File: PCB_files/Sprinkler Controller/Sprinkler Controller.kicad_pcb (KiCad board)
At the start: 2 copper layers, 1 part, among them U1 ESP32_DevKit_V1_DOIT

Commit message: progress on PCB
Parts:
- added BR1: DF04S, Bridge_rectifier:SOP510P1040X260-4N, F.Cu at (116.3, 89.0)
- added C1: 1000 uF, Capacitor_THT:CP_Radial_D12.5mm_P5.00mm, F.Cu at (115.0, 99.3)
- added D1: SS34, Diode_SMD:D_SMA, F.Cu at (131.0, 103.8)
- added J1: Screw_Terminal_01x02, TerminalBlock_MetzConnect:TerminalBlock_MetzConnect_Type094_RT03502HBLU_1x02_P5.00mm_Horizontal, F.Cu at (104.0, 87.0)
- added J2: Screw_Terminal_01x11, TerminalBlock_Phoenix:TerminalBlock_Phoenix_MKDS-1,5-11_1x11_P5.00mm_Horizontal, F.Cu at (159.5, 146.5)
- added L1: 33uH, Inductor_SMD:L_Vishay_IHLP-5050, F.Cu at (145.5, 89.8)
- added RN1: 4816P-T02-681LF, Resistor_Network:SOIC127P762X240-16N, F.Cu at (173.0, 121.5)
- added RN2: 4816P-T02-681LF, Resistor_Network:SOIC127P762X240-16N, F.Cu at (197.0, 121.5)
- added U10: ~, SSR:OR-M4XXA, F.Cu at (202.0, 132.5)
- added U11: ~, SSR:OR-M4XXA, F.Cu at (207.0, 132.5)
- added U12: LM2596S-ADJ, Package_TO_SOT_SMD:TO-263-5_TabPin3, F.Cu at (130.1, 90.1)
- added U2: ~, SSR:OR-M4XXA, F.Cu at (162.0, 132.5)
- added U3: ~, SSR:OR-M4XXA, F.Cu at (167.0, 132.5)
- added U4: ~, SSR:OR-M4XXA, F.Cu at (172.0, 132.5)
- added U5: ~, SSR:OR-M4XXA, F.Cu at (177.0, 132.5)
- added U6: ~, SSR:OR-M4XXA, F.Cu at (182.0, 132.5)
- added U7: ~, SSR:OR-M4XXA, F.Cu at (187.0, 132.5)
- added U8: ~, SSR:OR-M4XXA, F.Cu at (192.0, 132.5)
- added U9: ~, SSR:OR-M4XXA, F.Cu at (197.0, 132.5)
- moved U1 42.2 mm to (164.3, 97.5), turned to 90 degrees
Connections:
- U1 pad 10: unconnected-(U1-IO27-Pad10) -> Net-(U1-IO27)
- U1 pad 11: unconnected-(U1-IO14-Pad11) -> Net-(U1-IO14)
- U1 pad 13: unconnected-(U1-IO13-Pad13) -> Net-(U1-IO13)
- U1 pad 24: unconnected-(U1-IO18-Pad24) -> Net-(U1-IO18)
- U1 pad 25: unconnected-(U1-IO19-Pad25) -> Net-(U1-IO19)
- U1 pad 26: unconnected-(U1-IO21-Pad26) -> Net-(U1-IO21)
- U1 pad 6: unconnected-(U1-IO32-Pad6) -> Net-(U1-IO32)
- U1 pad 7: unconnected-(U1-IO33-Pad7) -> Net-(U1-IO33)
- U1 pad 8: unconnected-(U1-IO25-Pad8) -> Net-(U1-IO25)
- U1 pad 9: unconnected-(U1-IO26-Pad9) -> Net-(U1-IO26)
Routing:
- net Net-(U1-IO27): track 0.00 -> 18.2 mm, vias 0 -> 1
- net Net-(U1-IO26): track 0.00 -> 17.0 mm
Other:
- board outline added: 116 x 72 mm

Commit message: board complete
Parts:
- added C2: 220uF, Capacitor_THT:CP_Radial_D10.0mm_P5.00mm, F.Cu at (152.5, 99.6)
- added C3: 0.1uF, Capacitor_SMD:C_0603_1608Metric, F.Cu at (123.5, 104.2)
- added C4: 0.0033uF, Capacitor_SMD:C_0402_1005Metric, F.Cu at (136.5, 98.5)
- added C5: 0.1uF, Capacitor_SMD:C_0603_1608Metric, F.Cu at (138.0, 99.0)
- added D10: LED, LED_SMD:LED_0402_1005Metric, F.Cu at (197.0, 130.0)
- added D11: LED, LED_SMD:LED_0402_1005Metric, F.Cu at (202.0, 130.0)
- added D12: LED, LED_SMD:LED_0402_1005Metric, F.Cu at (207.0, 130.0)
- added D2: LED, LED_SMD:LED_0402_1005Metric, F.Cu at (146.0, 105.5)
- added D3: LED, LED_SMD:LED_0402_1005Metric, F.Cu at (162.0, 130.0)
- added D4: LED, LED_SMD:LED_0402_1005Metric, F.Cu at (167.0, 130.0)
- added D5: LED, LED_SMD:LED_0402_1005Metric, F.Cu at (172.0, 130.0)
- added D6: LED, LED_SMD:LED_0402_1005Metric, F.Cu at (177.0, 130.0)
- added D7: LED, LED_SMD:LED_0402_1005Metric, F.Cu at (182.0, 130.0)
- added D8: LED, LED_SMD:LED_0402_1005Metric, F.Cu at (187.0, 130.0)
- added D9: LED, LED_SMD:LED_0402_1005Metric, F.Cu at (192.0, 130.0)
- added R1: 510, Resistor_SMD:R_0805_2012Metric, F.Cu at (137.0, 105.4)
- added R2: 1k, Resistor_SMD:R_1206_3216Metric, F.Cu at (146.0, 100.0)
- added RV1: 10k, Potentiometer:RES3_PV36W103C01B00_BRN, F.Cu at (142.0, 105.0)
- moved J2 0.50 mm to (159.0, 146.5)
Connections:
- BR1 pad 2: Net-(BR1--) -> GND
- BR1 pad 3: Net-(BR1-~_1) -> AC
- BR1 pad 4: Net-(BR1-~_2) -> GNDPWR
- C1 pad 2: Net-(BR1--) -> GND
- D1 pad 2: Net-(BR1--) -> GND
- J1 pad 1: Net-(BR1-~_1) -> AC
- J1 pad 2: Net-(BR1-~_2) -> GNDPWR
- J2 pad 11: Net-(BR1-~_1) -> GNDPWR
- L1 pad 2: unconnected-(L1-Pad2) -> VCC
- RN1 pad 11: Net-(U6-Input+) -> Net-(D7-A)
- RN1 pad 12: Net-(U5-Input+) -> Net-(D6-A)
- RN1 pad 13: Net-(U4-Input+) -> Net-(D5-A)
- RN1 pad 14: Net-(U3-Input+) -> Net-(D4-A)
- RN1 pad 15: Net-(U2-Input+) -> Net-(D3-A)
- RN2 pad 11: Net-(U11-Input+) -> Net-(D12-A)
- RN2 pad 12: Net-(U10-Input+) -> Net-(D11-A)
- RN2 pad 13: Net-(U9-Input+) -> Net-(D10-A)
- RN2 pad 14: Net-(U8-Input+) -> Net-(D9-A)
- RN2 pad 15: Net-(U7-Input+) -> Net-(D8-A)
- U1 pad 14: unconnected-(U1-GND-Pad14) -> GND
- U1 pad 15: unconnected-(U1-VIN-Pad15) -> VCC
- U1 pad 17: unconnected-(U1-GND-Pad17) -> GND
- U10 pad 1: Net-(U10-Input+) -> Net-(D11-K)
- U10 pad 3: Net-(BR1-~_2) -> AC
- U11 pad 1: Net-(U11-Input+) -> Net-(D12-K)
- U11 pad 3: Net-(BR1-~_2) -> AC
- U12 pad 3: Net-(BR1--) -> GND
- U12 pad 4: unconnected-(U12-FB-Pad4) -> Net-(U12-FB)
- U12 pad 5: Net-(BR1--) -> GND
- U2 pad 1: Net-(U2-Input+) -> Net-(D3-K)
- U2 pad 3: Net-(BR1-~_2) -> AC
- U3 pad 1: Net-(U3-Input+) -> Net-(D4-K)
- U3 pad 3: Net-(BR1-~_2) -> AC
- U4 pad 1: Net-(U4-Input+) -> Net-(D5-K)
- U4 pad 3: Net-(BR1-~_2) -> AC
- U5 pad 1: Net-(U5-Input+) -> Net-(D6-K)
- U5 pad 3: Net-(BR1-~_2) -> AC
- U6 pad 1: Net-(U6-Input+) -> Net-(D7-K)
- U6 pad 3: Net-(BR1-~_2) -> AC
- U7 pad 1: Net-(U7-Input+) -> Net-(D8-K)
- U7 pad 3: Net-(BR1-~_2) -> AC
- U8 pad 1: Net-(U8-Input+) -> Net-(D9-K)
- U8 pad 3: Net-(BR1-~_2) -> AC
- U9 pad 1: Net-(U9-Input+) -> Net-(D10-K)
- U9 pad 3: Net-(BR1-~_2) -> AC
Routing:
- net GNDPWR: track 0.00 -> 152.5 mm
- net GND: track 0.00 -> 103.2 mm, vias 0 -> 5
- net VCC: track 0.00 -> 82.4 mm, vias 0 -> 1
- net Net-(U1-IO19): track 0.00 -> 76.7 mm, vias 0 -> 2
- net Net-(U1-IO21): track 0.00 -> 53.6 mm, vias 0 -> 1
- net Net-(U1-IO18): track 0.00 -> 45.6 mm, vias 0 -> 1
- net Net-(U1-IO33): track 0.00 -> 29.9 mm, vias 0 -> 1
- net Net-(BR1-+): track 0.00 -> 29.4 mm
- net Net-(U1-IO32): track 0.00 -> 28.3 mm, vias 0 -> 1
- net Net-(D1-K): track 0.00 -> 23.7 mm
- net Net-(U1-IO25): track 0.00 -> 22.8 mm, vias 0 -> 1
- net Net-(U1-IO14): track 0.00 -> 22.6 mm, vias 0 -> 1
- net Net-(U1-IO13): track 0.00 -> 22.4 mm
- net Net-(D12-A): track 0.00 -> 21.1 mm, vias 0 -> 2
- net AC: track 0.00 -> 20.5 mm
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- added copper zone on F.Cu, net AC
- added copper zone on B.Cu, net GND
- added copper zone on F.Cu, net GND
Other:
- outline, holes or cut-outs redrawn

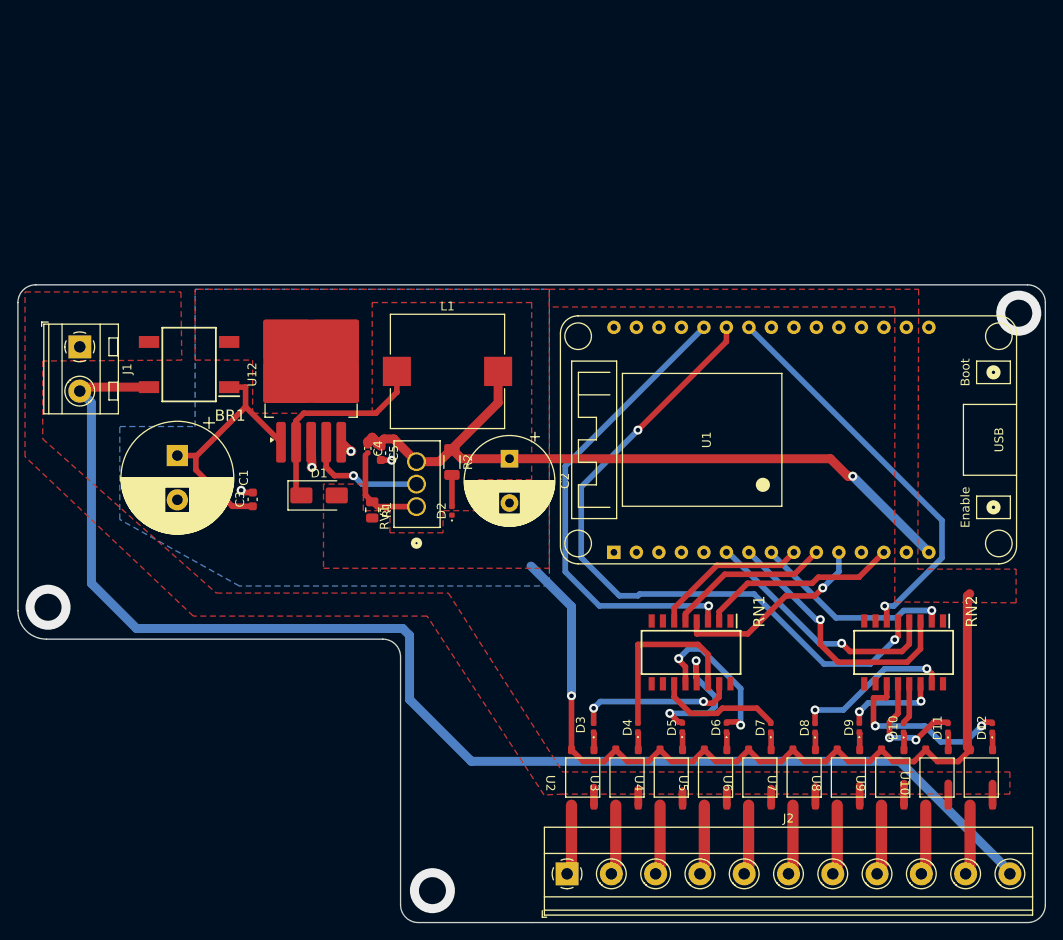
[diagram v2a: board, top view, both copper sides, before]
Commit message: fixed memory and logging issues
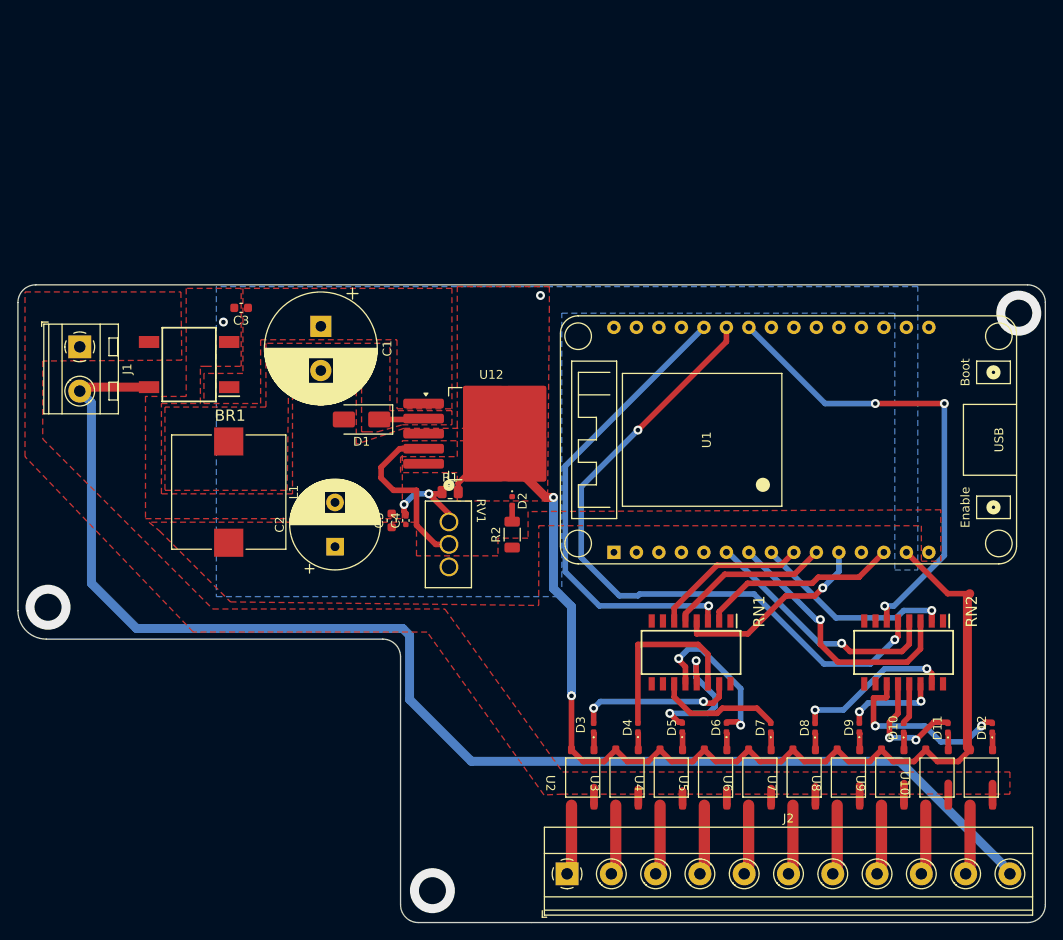
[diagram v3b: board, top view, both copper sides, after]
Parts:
- moved L1 28.2 mm to (120.8, 103.4), turned to -90 degrees
- moved C2 22.1 mm to (132.8, 109.6), turned to 90 degrees
- moved C1 21.8 mm to (131.2, 84.7)
- moved C3 21.7 mm to (122.2, 82.6), turned to 180 degrees
- moved U12 21.4 mm to (150.4, 96.8), turned to 0 degrees
- moved R2 10.7 mm to (152.8, 108.2), turned to 90 degrees
- moved D1 9.83 mm to (135.8, 95.2), turned to 180 degrees
- moved C4 9.19 mm to (140.8, 106.6), turned to 90 degrees
- moved R1 9.03 mm to (145.8, 103.4), turned to 0 degrees
- moved C5 7.69 mm to (139.2, 106.6), turned to 90 degrees
- moved D2 6.89 mm to (152.8, 104.4), turned to -90 degrees
- moved RV1 4.05 mm to (145.7, 106.8), turned to -90 degrees
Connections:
- net Net-(BR1-+) renamed /Vin
- net Net-(C4-Pad2) renamed /div
- net Net-(D1-K) renamed /Out
- net Net-(U12-FB) renamed /FB
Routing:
- net VCC: track 82.4 -> 0.00 mm, vias 1 -> 0
- net /Vin: track 29.4 -> 0.00 mm
- net GND: track 103.2 -> 122.5 mm, vias 5 -> 3
- net /Out: track 23.7 -> 5.04 mm
- net Net-(U1-IO18): track 45.6 -> 53.7 mm, vias 1 -> 3
- net /FB: track 13.8 -> 20.0 mm, vias 1 -> 0
- net Net-(D2-A): track 3.42 -> 1.70 mm
- net /div: track 11.2 -> 10.2 mm, vias 0 -> 2
- net (no net): vias 3 -> 4
- added copper zone on F.Cu, net /Out
- added copper zone on F.Cu, net /Vin
- added copper zone on F.Cu, net VCC
